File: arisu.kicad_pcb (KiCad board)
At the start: 2 copper layers, 339.1 x 118.7 mm, 176 parts, among them J1 USB_B_Micro, SW1 SW_Push, SW10 SW_Push, SW11 SW_Push, SW12 SW_Push, SW13 SW_Push, SW14 SW_Push, SW15 SW_Push, SW16 SW_Push, SW17 SW_Push, SW18 SW_Push, SW19 SW_Push, SW2 SW_Push, SW20 SW_Push, SW21 SW_Push, SW22 SW_Push, SW23 SW_Push, SW24 SW_Push, SW25 SW_Push, SW26 SW_Push, SW27 SW_Push, SW28 SW_Push, SW29 SW_Push, SW3 SW_Push, SW30 SW_Push, SW31 SW_Push, SW32 SW_Push, SW33 SW_Push, SW34 SW_Push, SW35 SW_Push, SW36 SW_Push, SW37 SW_Push, SW38 SW_Push, SW39 SW_Push, SW4 SW_Push, SW40 SW_Push, SW41 SW_Push, SW42 SW_Push, SW43 SW_Push, SW44 SW_Push, SW45 SW_Push, SW46 SW_Push, SW47 SW_Push, SW48 SW_Push, SW49 SW_Push, SW5 SW_Push, SW50 SW_Push, SW51 SW_Push, SW52 SW_Push, SW53 SW_Push, SW54 SW_Push, SW55 SW_Push, SW56 SW_Push, SW57 SW_Push, SW58 SW_Push, SW59 SW_Push, SW6 SW_Push, SW60 SW_Push, SW61 SW_Push, SW62 SW_Push, SW63 SW_Push, SW64 SW_Push, SW65 SW_Push, SW66 SW_Push, SW67 SW_Push, SW7 SW_Push, SW8 SW_Push, SW9 SW_Push, U1 USBLC6-2SC6, U2 ATmega32U4-AU, Y1 Crystal_GND24

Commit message: Convert to new kicad format
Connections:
- net /~RES~ renamed /~{RES}
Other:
- net class Default removed
- net class Power removed

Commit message: new layout
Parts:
- removed C1, C2: 22pF, Capacitors_SMD:C_0805_HandSoldering
- removed C3: 10uF, Capacitors_SMD:C_0805_HandSoldering
- removed C4: 1uF (±10%), Capacitors_SMD:C_0805_HandSoldering
- removed C5: 1uF, Capacitors_SMD:C_0805_HandSoldering
- removed C6, C7, C8, C9: 0.1uF, Capacitors_SMD:C_0805_HandSoldering
- removed D+: D+, Pin_Headers:Pin_Header_Straight_1x01_Pitch2.54mm
- removed D-: D-, Pin_Headers:Pin_Header_Straight_1x01_Pitch2.54mm
- removed D1, D11, D12, D13, D14, D15, D16, D17, D18, D19, D2, D20, D21, D22, D23, D24, D25, D26, D27, D28, D29, D3, D30, D31, D32, D33, D34, D35, D36, D37, D38, D39, D4, D40, D41, D42, D43, D44, D45, D46, D47, D48, D49, D5, D50, D51, D52, D53, D54, D55, D56, D57, D58, D59, D6, D60, D61, D62, D63, D64, D65, D66, D67, D8, D9: D, Diodes_SMD:D_SOD-123
- removed the D10 at (82.2, 41.0)
- removed G*** (x2): LOGO, arisu:arisu-logo
- removed GND (x2): GND, Pin_Headers:Pin_Header_Straight_1x01_Pitch2.54mm
- removed H3, H5, H8: MountingHole, Mounting_Holes:MountingHole_2.2mm_M2_Pad
- removed J1: USB_B_Micro, Connectors_USB:USB_Micro-B_Molex-105017-0001
- removed MISO: MISO, Pin_Headers:Pin_Header_Straight_1x01_Pitch2.54mm
- removed MOSI: MOSI, Pin_Headers:Pin_Header_Straight_1x01_Pitch2.54mm
- removed PF4: PF4, Pin_Headers:Pin_Header_Straight_1x01_Pitch2.54mm
- removed PF5: PF5, Pin_Headers:Pin_Header_Straight_1x01_Pitch2.54mm
- removed PF6: PF6, Pin_Headers:Pin_Header_Straight_1x01_Pitch2.54mm
- removed PF7: PF7, Pin_Headers:Pin_Header_Straight_1x01_Pitch2.54mm
- removed R1, R2: 22, Resistors_SMD:R_0805_HandSoldering
- removed R3, R4: 10K, Resistors_SMD:R_0805_HandSoldering
- removed RES: RES, Pin_Headers:Pin_Header_Straight_1x01_Pitch2.54mm
- removed SCK: SCK, Pin_Headers:Pin_Header_Straight_1x01_Pitch2.54mm
- removed the SW54 at (288.3, 86.3)
- removed the SW58 at (307.3, 110.2)
- removed the SW61 at (326.4, 91.1)
- removed the SW62 at (326.4, 110.2)
- removed the SW64 at (337.0, 24.4)
- removed the SW65 at (341.2, 43.5)
- removed SWR1: SW_Push, Buttons_Switches_SMD:SW_SPST_TL3342
- removed U1: USBLC6-2SC6, TO_SOT_Packages_SMD:SOT-23-6_Handsoldering
- removed U2: ATmega32U4-AU, Housings_QFP:TQFP-44_10x10mm_Pitch0.8mm
- removed VCC (x2): VCC, Pin_Headers:Pin_Header_Straight_1x01_Pitch2.54mm
- removed Y1: Crystal_GND24, Crystals:Crystal_SMD_SeikoEpson_FA238-4pin_3.2x2.5mm_HandSoldering
- added SW1: SW_Push, MX_Switch:SW_Cherry_MX_1.00u_PCB, F.Cu at (18.8, 29.2)
- added SW2: SW_Push, MX_Switch:SW_Cherry_MX_1.00u_PCB, F.Cu at (14.6, 48.2)
- added SW3: SW_Push, MX_Switch:SW_Cherry_MX_1.00u_PCB, F.Cu at (10.5, 67.3)
- added SW55: SW_Push, MX_Switch:SW_Cherry_MX_1.50u_PCB, F.Cu at (269.3, 105.4)
- added SW60: SW_Push, MX_Switch:SW_Cherry_MX_1.50u_PCB, F.Cu at (297.8, 105.4)
- added SW8: SW_Push, MX_Switch:SW_Cherry_MX_1.50u_PCB, F.Cu at (25.4, 105.4)
- SW59: footprint MX_Switch:SW_Cherry_MX_1.00u_PCB -> MX_Switch:SW_Cherry_MX_2.00u_PCB_ReversedStabilizers
- SW63: footprint MX_Switch:SW_Cherry_MX_1.00u_PCB -> MX_Switch:SW_Cherry_MX_2.00u_PCB
- moved H1 274.5 mm to (321.3, -25.4)
- moved H6 126.6 mm to (306.1, 12.1)
- moved SW59 57.4 mm to (288.3, 86.3)
- moved H7 34.4 mm to (323.8, 13.8)
- moved SW66 30.5 mm to (326.4, 86.3)
- moved SW13 28.6 mm to (54.0, 105.4)
- moved SW67 19.6 mm to (326.4, 105.4)
- moved SW63 19.1 mm to (294.1, 29.2)
- renumbered D7 to D10, SW7 to SW10, SW8 to SW11, SW9 to SW12, SW5 to SW13, SW10 to SW14, SW11 to SW15, SW12 to SW16, SW13 to SW17, SW14 to SW18, SW15 to SW19, SW16 to SW20, SW17 to SW21, SW18 to SW22, SW19 to SW23, SW20 to SW24, SW21 to SW25, SW22 to SW26, SW23 to SW27, SW24 to SW28, SW25 to SW29, SW26 to SW30, SW27 to SW31, SW28 to SW32, SW29 to SW33, SW30 to SW34, SW31 to SW35, SW32 to SW36, SW33 to SW38, SW34 to SW39, SW1 to SW4, SW35 to SW40, SW36 to SW41, SW38 to SW42, SW39 to SW43, SW40 to SW44, SW41 to SW45, SW42 to SW47, SW43 to SW48, SW44 to SW49, SW2 to SW5, SW45 to SW50, SW47 to SW51, SW48 to SW52, SW49 to SW53, SW50 to SW54, SW51 to SW56, SW52 to SW57, SW53 to SW58, SW3 to SW6, SW55 to SW61, SW56 to SW62, SW60 to SW64, SW57 to SW65, SW4 to SW7, SW6 to SW9
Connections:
- SW13 pad 1: /col0 -> /col1
- SW34 pad 1: /col6 -> Net-(SW34-Pad1)
- SW35 pad 1: /col6 -> Net-(SW34-Pad1)
- SW36 pad 1: /col6 -> Net-(SW34-Pad1)
- SW37 pad 1: /SCK -> Net-(SW34-Pad1)
- SW46 pad 1: /col9 -> /col8
- SW59 pad 1: /col13 -> /col11
- SW63 pad 1: /MISO -> /col13
- SW65 pad 1: /col12 -> /col13
- SW66 pad 1: /MISO -> /col13
- SW67 pad 1: /MISO -> /col13
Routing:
- net /row4: track 433.8 -> 0.00 mm, vias 2 -> 0
- net /row3: track 432.5 -> 0.00 mm, vias 2 -> 0
- net /row2: track 399.4 -> 0.00 mm, vias 4 -> 0
- net /row1: track 384.1 -> 0.00 mm, vias 4 -> 0
- net /row0: track 328.0 -> 0.00 mm, vias 4 -> 0
- net /MISO: track 272.2 -> 0.00 mm, vias 1 -> 0
- net /col12: track 249.0 -> 24.7 mm
- net VCC: track 205.4 -> 0.00 mm, vias 9 -> 0
- net /col13: track 269.0 -> 88.0 mm
- net /col11: track 230.6 -> 97.0 mm
- net /col10: track 221.3 -> 90.1 mm
- net /col0: track 204.4 -> 80.3 mm
- net /col6: track 96.8 -> 0.00 mm
- net /SCK: track 157.0 -> 64.6 mm, vias 2 -> 0
- net /col2: track 175.7 -> 87.4 mm, vias 2 -> 0
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- added copper zone on B.Cu, net (none)
- added copper zone on F.Cu, net (none)
- removed copper zone on B.Cu, net GND
- removed copper zone on F.Cu, net GND
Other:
- board size 339.1 x 118.7 mm -> 343 x 119 mm
- board text added: "Concept outline, not final"

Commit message: scripting tests
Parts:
- added D1: D, Diode_SMD:D_SOD-123, B.Cu at (18.8, 29.2)
- added D11: D, Diode_SMD:D_SOD-123, B.Cu at (62.9, 67.3)
- added D12: D, Diode_SMD:D_SOD-123, B.Cu at (68.3, 86.3)
- added D13: D, Diode_SMD:D_SOD-123, B.Cu at (54.0, 105.4)
- added D14: D, Diode_SMD:D_SOD-123, B.Cu at (75.9, 27.7)
- added D15: D, Diode_SMD:D_SOD-123, B.Cu at (84.9, 46.8)
- added D16: D, Diode_SMD:D_SOD-123, B.Cu at (85.6, 66.4)
- added D17: D, Diode_SMD:D_SOD-123, B.Cu at (91.0, 87.0)
- added D18: D, Diode_SMD:D_SOD-123, B.Cu at (87.0, 105.7)
- added D19: D, Diode_SMD:D_SOD-123, B.Cu at (98.2, 30.1)
- added D2: D, Diode_SMD:D_SOD-123, B.Cu at (14.6, 48.2)
- added D20: D, Diode_SMD:D_SOD-123, B.Cu at (103.5, 50.8)
- added D21: D, Diode_SMD:D_SOD-123, B.Cu at (104.2, 70.4)
- added D22: D, Diode_SMD:D_SOD-123, B.Cu at (109.6, 91.0)
- added D23: D, Diode_SMD:D_SOD-123, B.Cu at (116.8, 34.1)
- added D24: D, Diode_SMD:D_SOD-123, B.Cu at (122.2, 54.7)
- added D25: D, Diode_SMD:D_SOD-123, B.Cu at (122.9, 74.3)
- added D26: D, Diode_SMD:D_SOD-123, B.Cu at (128.2, 95.0)
- added D27: D, Diode_SMD:D_SOD-123, B.Cu at (115.0, 111.6)
- added D28: D, Diode_SMD:D_SOD-123, B.Cu at (135.5, 38.1)
- added D29: D, Diode_SMD:D_SOD-123, B.Cu at (140.8, 58.7)
- added D3: D, Diode_SMD:D_SOD-123, B.Cu at (10.5, 67.3)
- added D30: D, Diode_SMD:D_SOD-123, B.Cu at (141.5, 78.3)
- added D31: D, Diode_SMD:D_SOD-123, B.Cu at (146.9, 98.9)
- added D32: D, Diode_SMD:D_SOD-123, B.Cu at (152.2, 119.5)
- added D33: D, Diode_SMD:D_SOD-123, B.Cu at (154.1, 42.0)
- added D34: D, Diode_SMD:D_SOD-123, B.Cu at (172.9, 66.6)
- added D35: D, Diode_SMD:D_SOD-123, B.Cu at (181.6, 84.2)
- added D36: D, Diode_SMD:D_SOD-123, B.Cu at (190.2, 101.9)
- added D37: D, Diode_SMD:D_SOD-123, B.Cu at (184.8, 122.5)
- added D38: D, Diode_SMD:D_SOD-123, B.Cu at (178.3, 46.0)
- added D39: D, Diode_SMD:D_SOD-123, B.Cu at (191.6, 62.6)
- added D4: D, Diode_SMD:D_SOD-123, B.Cu at (37.8, 29.2)
- added D40: D, Diode_SMD:D_SOD-123, B.Cu at (200.2, 80.3)
- added D41: D, Diode_SMD:D_SOD-123, B.Cu at (208.8, 97.9)
- added D42: D, Diode_SMD:D_SOD-123, B.Cu at (196.9, 42.0)
- added D43: D, Diode_SMD:D_SOD-123, B.Cu at (210.2, 58.7)
- added D44: D, Diode_SMD:D_SOD-123, B.Cu at (218.8, 76.3)
- added D45: D, Diode_SMD:D_SOD-123, B.Cu at (227.4, 94.0)
- added D46: D, Diode_SMD:D_SOD-123, B.Cu at (236.1, 111.6)
- added D47: D, Diode_SMD:D_SOD-123, B.Cu at (215.6, 38.1)
- added D48: D, Diode_SMD:D_SOD-123, B.Cu at (228.8, 54.7)
- added D49: D, Diode_SMD:D_SOD-123, B.Cu at (237.5, 72.4)
- added D5: D, Diode_SMD:D_SOD-123, B.Cu at (33.7, 48.2)
- added D50: D, Diode_SMD:D_SOD-123, B.Cu at (246.1, 90.0)
- added D51: D, Diode_SMD:D_SOD-123, B.Cu at (234.2, 34.1)
- added D52: D, Diode_SMD:D_SOD-123, B.Cu at (247.5, 50.8)
- added D53: D, Diode_SMD:D_SOD-123, B.Cu at (259.7, 67.3)
- added D54: D, Diode_SMD:D_SOD-123, B.Cu at (269.3, 86.3)
- added D55: D, Diode_SMD:D_SOD-123, B.Cu at (269.3, 105.4)
- added D56: D, Diode_SMD:D_SOD-123, B.Cu at (256.0, 27.7)
- added D57: D, Diode_SMD:D_SOD-123, B.Cu at (269.7, 48.2)
- added D58: D, Diode_SMD:D_SOD-123, B.Cu at (278.8, 67.3)
- added D59: D, Diode_SMD:D_SOD-123, B.Cu at (288.3, 86.3)
- added D6: D, Diode_SMD:D_SOD-123, B.Cu at (29.6, 67.3)
- added D60: D, Diode_SMD:D_SOD-123, B.Cu at (297.8, 105.4)
- added D61: D, Diode_SMD:D_SOD-123, B.Cu at (275.1, 29.2)
- added D62: D, Diode_SMD:D_SOD-123, B.Cu at (288.8, 48.2)
- added D63: D, Diode_SMD:D_SOD-123, B.Cu at (294.1, 29.2)
- added D64: D, Diode_SMD:D_SOD-123, B.Cu at (307.8, 48.2)
- added D65: D, Diode_SMD:D_SOD-123, B.Cu at (297.8, 67.3)
- added D66: D, Diode_SMD:D_SOD-123, B.Cu at (326.4, 86.3)
- added D67: D, Diode_SMD:D_SOD-123, B.Cu at (326.4, 105.4)
- added D7: D, Diode_SMD:D_SOD-123, B.Cu at (25.4, 86.3)
- added D8: D, Diode_SMD:D_SOD-123, B.Cu at (25.4, 105.4)
- added D9: D, Diode_SMD:D_SOD-123, B.Cu at (56.9, 29.2)
- D10: footprint Diodes_SMD:D_SOD-123 -> Diode_SMD:D_SOD-123
- moved D10 14.7 mm to (62.2, 48.2), turned to 180 degrees

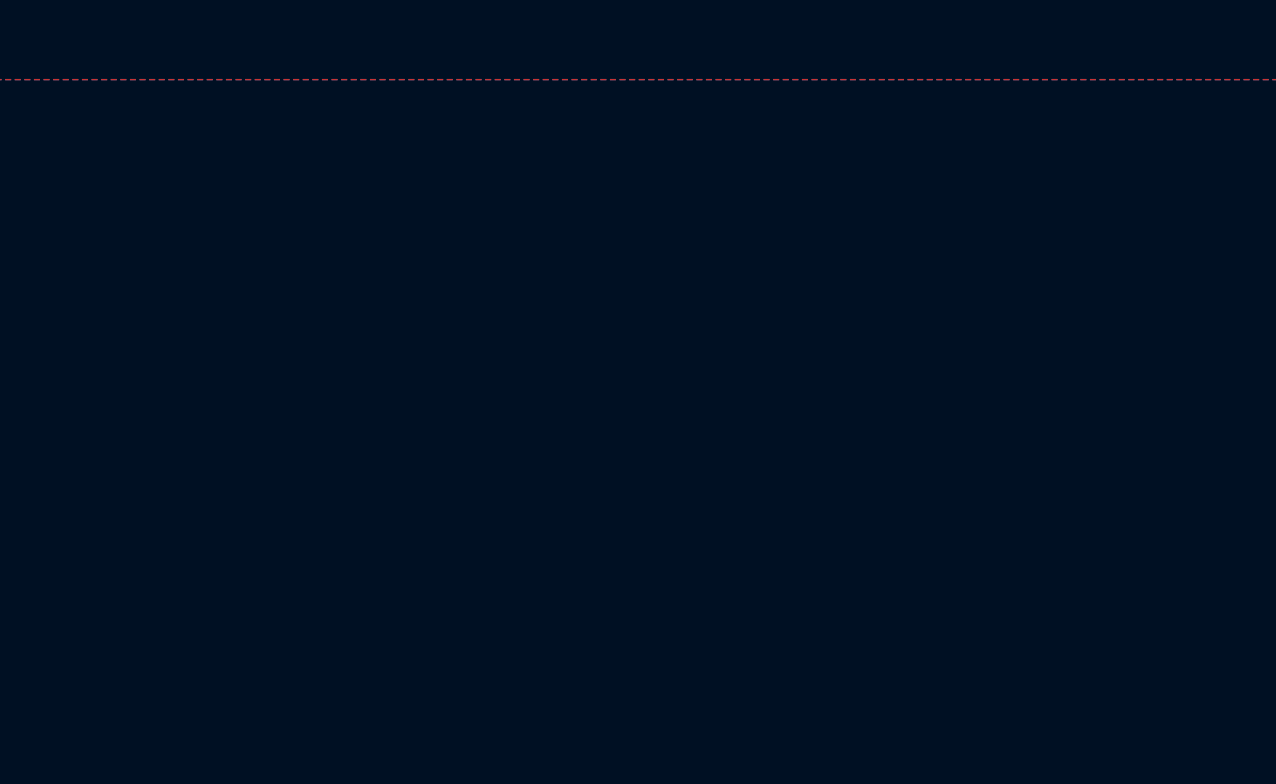
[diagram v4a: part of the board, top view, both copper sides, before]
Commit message: Add RP2040
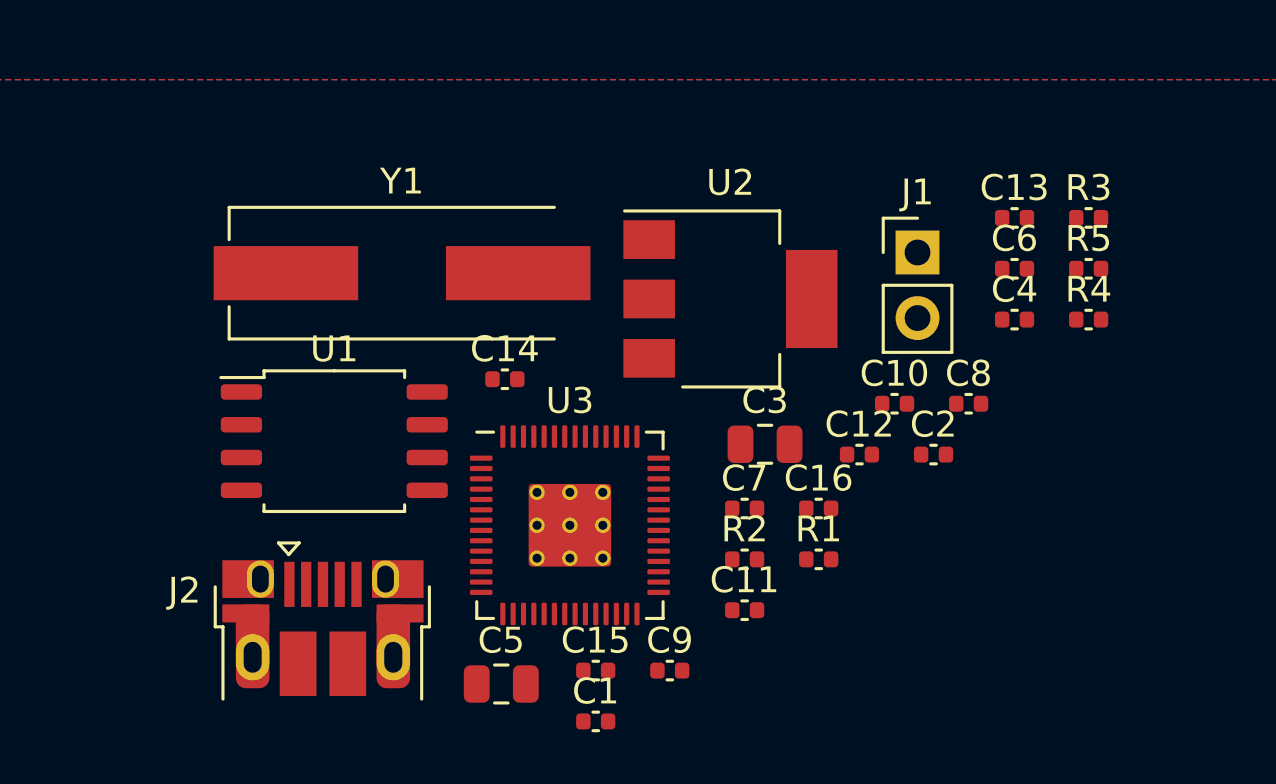
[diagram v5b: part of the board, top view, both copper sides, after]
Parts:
- added C1: 27p, Capacitor_SMD:C_0402_1005Metric, F.Cu at (56.1, 169.7)
- added C10: 1u, Capacitor_SMD:C_0402_1005Metric, F.Cu at (67.7, 157.3)
- added C11: 100n, Capacitor_SMD:C_0402_1005Metric, F.Cu at (61.9, 165.3)
- added C12: 100n, Capacitor_SMD:C_0402_1005Metric, F.Cu at (66.4, 159.3)
- added C13: 100n, Capacitor_SMD:C_0402_1005Metric, F.Cu at (72.4, 150.1)
- added C14: 100n, Capacitor_SMD:C_0402_1005Metric, F.Cu at (52.6, 156.4)
- added C15: 100n, Capacitor_SMD:C_0402_1005Metric, F.Cu at (56.1, 167.7)
- added C16: 100n, Capacitor_SMD:C_0402_1005Metric, F.Cu at (64.8, 161.4)
- added C2: 27p, Capacitor_SMD:C_0402_1005Metric, F.Cu at (69.2, 159.3)
- added C3: 10u, Capacitor_SMD:C_0805_2012Metric, F.Cu at (62.7, 158.9)
- added C4: 100n, Capacitor_SMD:C_0402_1005Metric, F.Cu at (72.4, 154.1)
- added C5: 10u, Capacitor_SMD:C_0805_2012Metric, F.Cu at (52.5, 168.2)
- added C6: 100n, Capacitor_SMD:C_0402_1005Metric, F.Cu at (72.4, 152.1)
- added C7: 100n, Capacitor_SMD:C_0402_1005Metric, F.Cu at (61.9, 161.4)
- added C8: 1u, Capacitor_SMD:C_0402_1005Metric, F.Cu at (70.6, 157.3)
- added C9: 100n, Capacitor_SMD:C_0402_1005Metric, F.Cu at (59.0, 167.7)
- added J1: Conn_01x02, Connector_PinHeader_2.54mm:PinHeader_1x02_P2.54mm_Vertical, F.Cu at (68.6, 151.5)
- added J2: USB_B_Micro, RP2040_minimal:USB_Micro-B_Amphenol_10103594-0001LF_Horizontal_modified, F.Cu at (45.6, 167.2)
- added R1: 1k, Capacitor_SMD:C_0402_1005Metric, F.Cu at (64.8, 163.4)
- added R2: DNF, Capacitor_SMD:C_0402_1005Metric, F.Cu at (61.9, 163.4)
- added R3: 1k, Capacitor_SMD:C_0402_1005Metric, F.Cu at (75.2, 150.1)
- added R4: 27, Capacitor_SMD:C_0402_1005Metric, F.Cu at (75.2, 154.1)
- added R5: 27, Capacitor_SMD:C_0402_1005Metric, F.Cu at (75.2, 152.1)
- added U1: W25Q128JVS, Package_SO:SOIC-8_5.23x5.23mm_P1.27mm, F.Cu at (46.0, 158.8)
- added U2: NCP1117-3.3_SOT223, Package_TO_SOT_SMD:SOT-223-3_TabPin2, F.Cu at (61.4, 153.3)
- added U3: RP2040, RP2040_minimal:RP2040-QFN-56, F.Cu at (55.1, 162.1)
- added Y1: ABLS-12.000MHZ-B4-T, RP2040_minimal:Crystal_SMD_HC49-US, F.Cu at (48.6, 152.3)
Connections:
- net /SCK renamed /col7
